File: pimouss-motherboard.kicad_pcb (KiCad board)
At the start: 4 copper layers, 281 parts, among them J1 Conn_02x10_Odd_Even, J10 Barrel_Jack_Switch, J2 TMS-105-57-GD, J3 Conn_02x10_Odd_Even, J4 Conn_01x03_Male, J5 Micro_SD_Card_Det, J9 RJSAE-5x8, P1 QSH-060-01-L-D-A, P2 PCIE-064-02, P3 MPCIE-Socket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

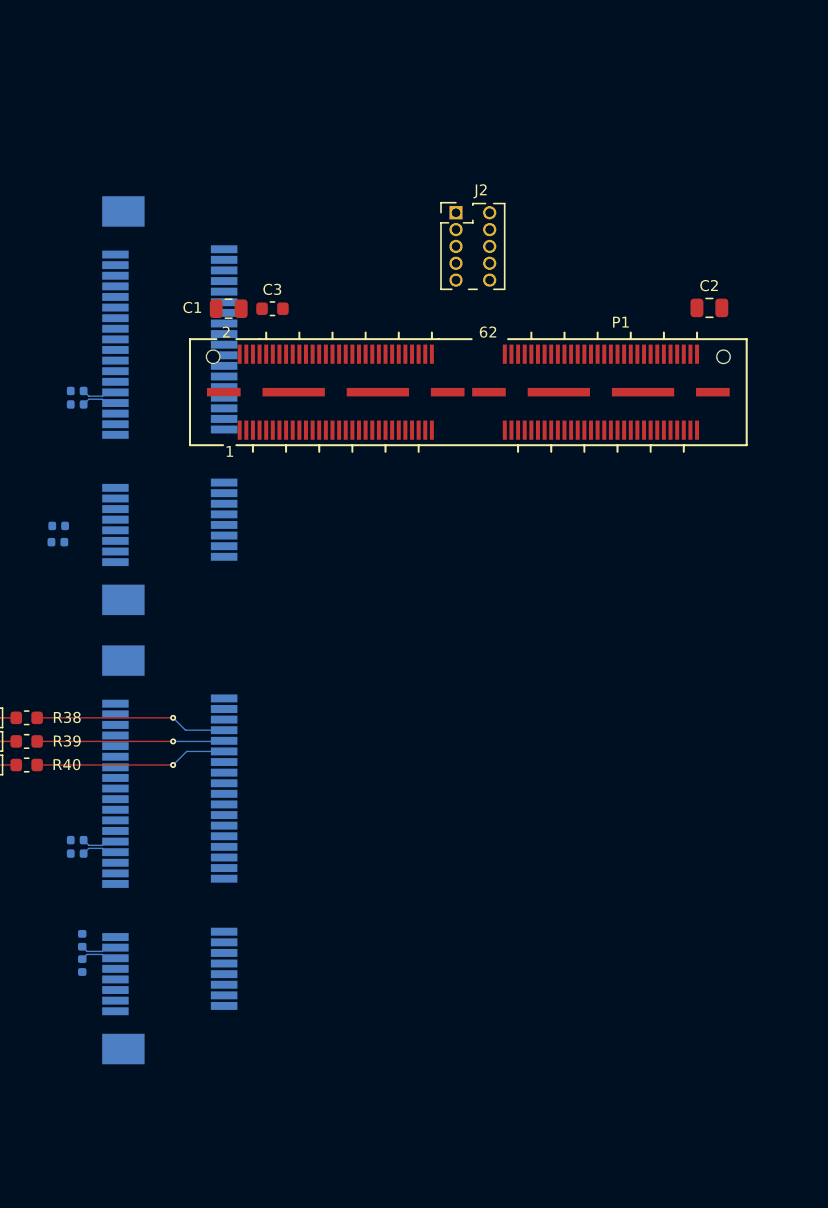
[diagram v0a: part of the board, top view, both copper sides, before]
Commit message: sch, master: Add pimouss SoM component
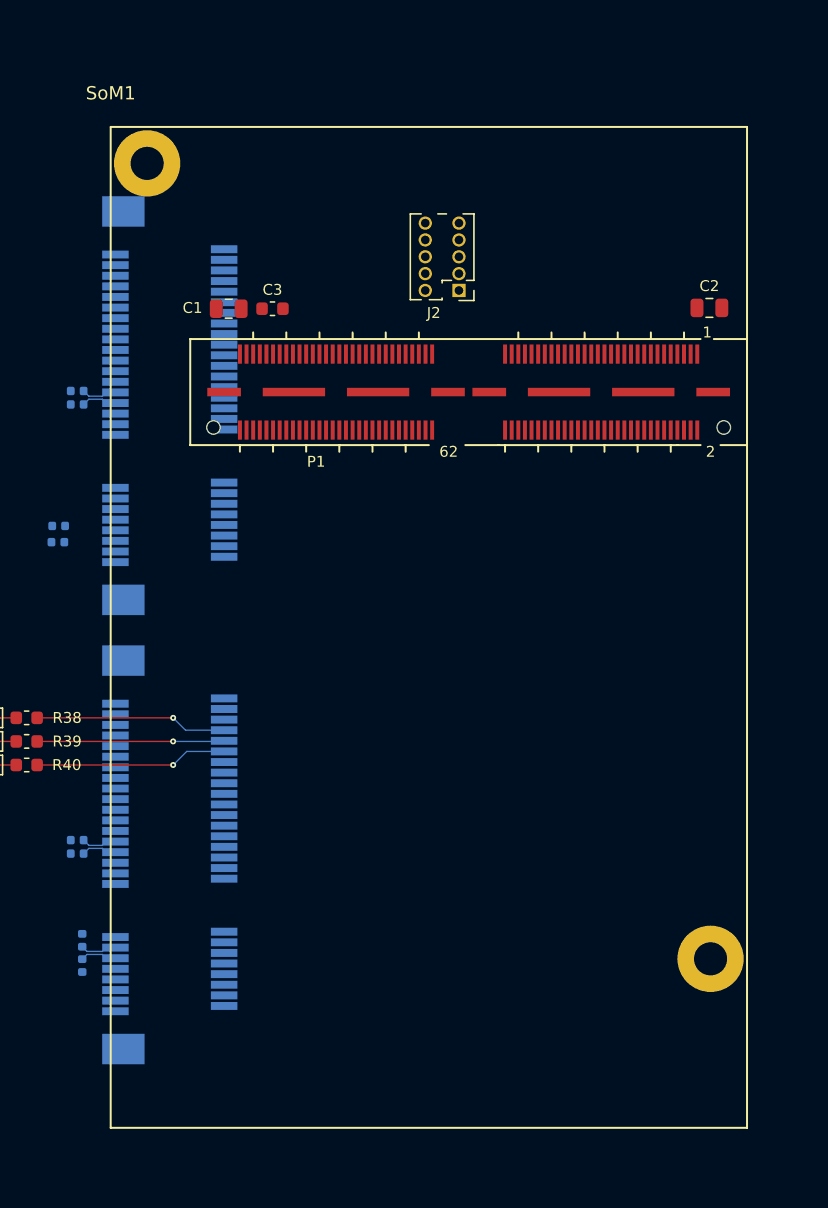
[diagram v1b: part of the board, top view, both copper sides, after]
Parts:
- added SoM1: Pimouss, pimouss-motherboard:Pimouss, F.Cu at (131.9, 58.7)
- moved J2 2.45 mm to (129.9, 48.5), turned to 180 degrees
- turned P1 to 180 degrees

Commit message: pcb: Place all components on the board
only routing left...
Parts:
- removed C14, C17, C21, C22, C24, C25: 1u, Capacitor_SMD:C_0603_1608Metric
- removed L3, L5, L6: 600@100M, Inductor_SMD:L_0603_1608Metric
- removed Q1: DMP2040USS, Package_SO:SOIC-8_3.9x4.9mm_P1.27mm
- added REF**: mpcie_card_left, pimouss-motherboard:mpcie_card_left, B.Cu at (103.9, 73.4)
- added REF**: mpcie_card_left, pimouss-motherboard:mpcie_card_left, B.Cu at (103.9, 107.3)
- added REF**: pcie_x4_card, pimouss-motherboard:pcie_x4_card, F.Cu at (162.6, 80.8)
- added REF**: PTH_3.3_6, pimouss-motherboard:PTH_3.3_6, F.Cu at (163.9, 26.3)
- added REF**: PTH_3.3_6, pimouss-motherboard:PTH_3.3_6, F.Cu at (163.9, 138.3)
- added REF**: PTH_3.3_6, pimouss-motherboard:PTH_3.3_6, F.Cu at (101.9, 138.3)
- added REF**: PTH_3.3_6, pimouss-motherboard:PTH_3.3_6, F.Cu at (101.9, 26.3)
- C20, C23, C40, C49, C50, C51, C52, C53, C54, C55, C56, L10, L11, L12, L4, L9: moved to B.Cu
- moved R4 164.8 mm to (114.5, 69.5), turned to 180 degrees
- moved R3 161.0 mm to (111.2, 67.9)
- moved R5 160.4 mm to (114.5, 71.4), turned to 180 degrees
- moved C108 157.1 mm to (120.3, 49.6), turned to 270 degrees
- moved R74 155.9 mm to (122.6, 50.3), turned to 180 degrees
- moved C112 155.6 mm to (122.6, 48.8), turned to 180 degrees
- moved R7 154.7 mm to (114.5, 66.6)
- moved C106 146.8 mm to (127.8, 43.3), turned to 270 degrees
- moved R9 145.3 mm to (121.0, 66.2)
- moved P5 144.1 mm to (112.6, 22.0), turned to 180 degrees
- moved R8 143.4 mm to (121.0, 64.7)
- moved R75 143.3 mm to (122.6, 51.8)
- moved U1 143.1 mm to (111.1, 70.5)
- moved C36 142.1 mm to (111.6, 32.4), turned to 180 degrees
- moved R10 141.6 mm to (128.1, 53.1)
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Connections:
- C120 pad 1: /pcie/switch/VDDR -> /pcie/switch/AVDDH
- C122 pad 1: /pcie/switch/VDDR -> /pcie/switch/AVDDH
- C124 pad 1: /pcie/switch/VDDR -> /pcie/switch/AVDDH
- C126 pad 1: /pcie/switch/VDDR -> /pcie/switch/AVDDH
- C128 pad 1: /pcie/switch/VDDR -> /pcie/switch/AVDDH
- C130 pad 1: /pcie/switch/VDDR -> /pcie/switch/AVDDH
- C139 pad 1: /pcie/switch/VDDCAUX -> /pcie/switch/AVDD
- C141 pad 1: /pcie/switch/VDDCAUX -> /pcie/switch/AVDD
- C143 pad 1: /pcie/switch/VDDCAUX -> /pcie/switch/AVDD
- C145 pad 1: /pcie/switch/CVDDR -> /pcie/switch/AVDDH
- C147 pad 1: /pcie/switch/CVDDR -> /pcie/switch/AVDDH
- C149 pad 1: /pcie/switch/CVDDR -> /pcie/switch/AVDDH
- C150 pad 1: /pcie/switch/CVDDR -> /pcie/switch/AVDDH
- C16 pad 1: /pcie/switch/VDDCAUX -> /pcie/switch/AVDD
- C23 pad 1: /pcie/switch/VDDR -> /pcie/switch/AVDDH
- J10 pad 1: Net-(J10-Pad1) -> +12V
- L2 pad 2: /pcie/switch/VDDCAUX -> /pcie/switch/AVDD
- L4 pad 2: /pcie/switch/VDDR -> /pcie/switch/AVDDH
- U2 pad 1: /pcie/switch/VDDR -> /pcie/switch/AVDDH
- U2 pad 13: /pcie/switch/VDDCAUX -> /pcie/switch/AVDD
- U2 pad 14: /pcie/switch/VDDCAUX -> /pcie/switch/AVDD
- U2 pad 49: /pcie/switch/VDDR -> /pcie/switch/AVDDH
- U2 pad 64: /pcie/switch/VDDR -> /pcie/switch/AVDDH
- U2 pad 79: /pcie/switch/CVDDR -> /pcie/switch/AVDDH
- U2 pad 8: /pcie/switch/VDDR -> /pcie/switch/AVDDH
- U2 pad 82: /pcie/switch/CVDDR -> /pcie/switch/AVDDH
- U2 pad 84: /pcie/switch/CVDDR -> /pcie/switch/AVDDH
- U2 pad 96: /pcie/switch/VDDR -> /pcie/switch/AVDDH
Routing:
- net /pcie/TX_O2_N: track 0.00 -> 60.4 mm
- net /pcie/TX_O2_P: track 0.00 -> 60.3 mm
- net /pcie/switch/AVDDH: track 23.1 -> 82.9 mm, vias 2 -> 11
- net /pcie/CLK_O2_N: track 0.00 -> 58.8 mm, vias 0 -> 2
- net /pcie/CLK_O2_P: track 0.00 -> 58.0 mm, vias 0 -> 2
- net /pcie/switch/VDDR: track 55.4 -> 0.00 mm, vias 5 -> 0
- net /pcie/CLK_O1_N: track 2.77 -> 39.0 mm
- net /pcie/CLK_O1_P: track 2.77 -> 38.6 mm
- net /phy_adm/REF_CLK_P: track 0.00 -> 32.9 mm
- net /phy_adm/REF_CLK_N: track 0.00 -> 32.8 mm
- net /pcie/TX_O1_N: track 0.00 -> 31.8 mm
- net /pcie/TX_O1_P: track 0.00 -> 31.1 mm
- net /pcie/switch/REFCLK_N: track 6.79 -> 33.5 mm, vias 0 -> 2
- net /pcie/switch/REFCLK_P: track 6.79 -> 32.3 mm, vias 0 -> 2
- net /pcie/RX_O2_P: track 6.75 -> 31.7 mm
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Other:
- board outline added: 70 x 120 mm

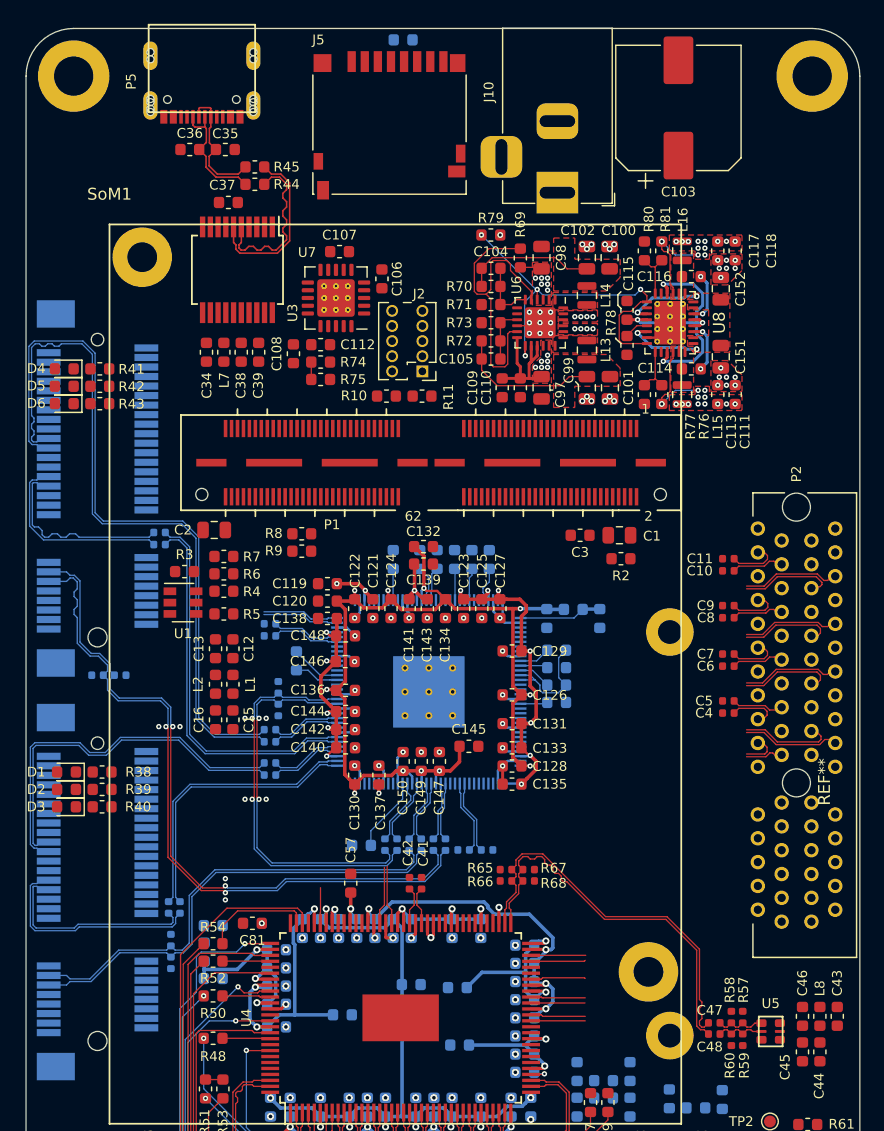
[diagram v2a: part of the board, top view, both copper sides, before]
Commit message: pcb: Routed PCIe differential tracks
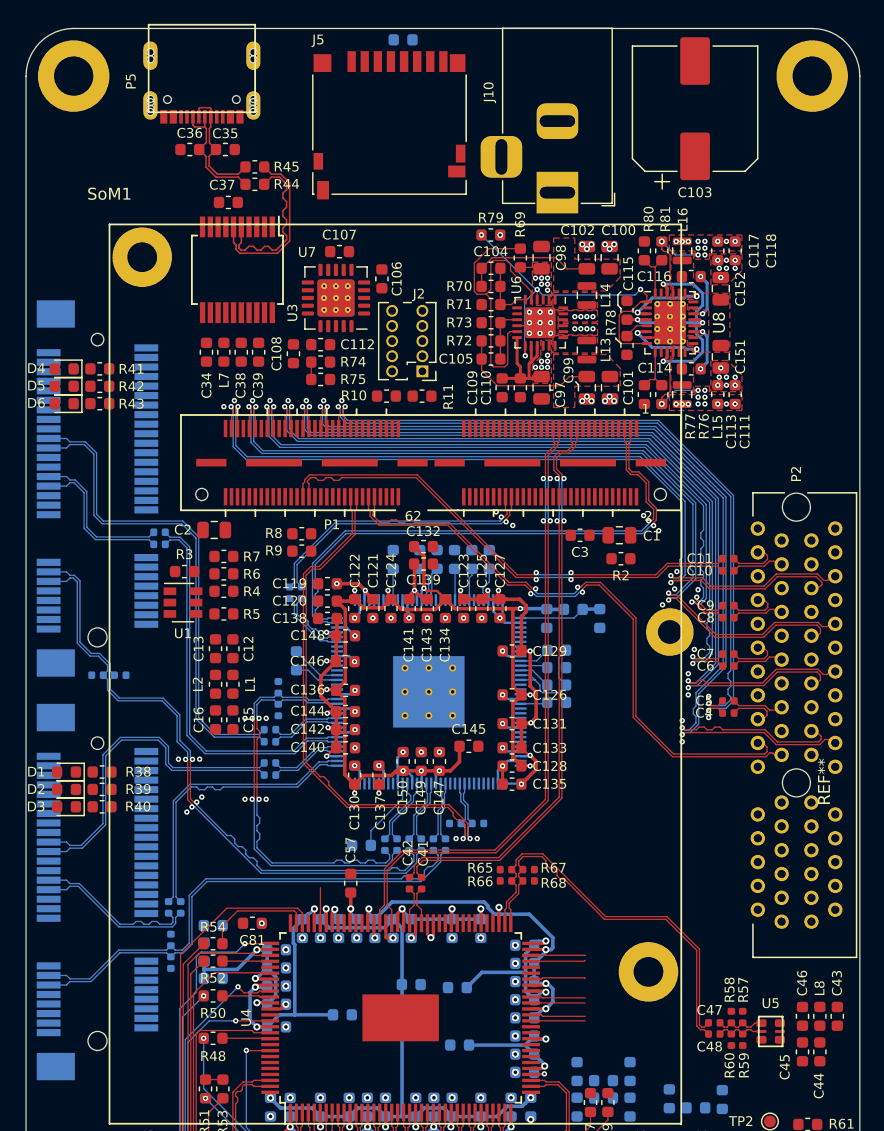
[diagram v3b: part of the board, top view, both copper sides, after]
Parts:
- removed the REF** at (103.9, 107.3)
- moved R24 24.9 mm to (103.9, 76.6), turned to 180 degrees
- moved R22 24.9 mm to (110.0, 100.7), turned to 270 degrees
- moved R25 22.6 mm to (105.8, 76.6), turned to 0 degrees
- moved R23 22.6 mm to (110.0, 98.8), turned to 90 degrees
- moved C19 3.98 mm to (120.0, 69.7), turned to 90 degrees
- moved C18 3.73 mm to (121.0, 69.7), turned to 90 degrees
- moved R14 2.35 mm to (135.8, 89.0)
- moved R16 2.33 mm to (133.9, 89.0)
- moved C103 1.40 mm to (154.1, 29.0)
- moved C32 1.04 mm to (109.1, 64.6)
- moved C31 1.02 mm to (110.9, 96.1)
- moved C33 1.00 mm to (109.1, 65.6)
- moved C30 0.95 mm to (109.9, 96.1)
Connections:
- C30 pad 1: /pcie/RX_O1_P -> /pcie/RX_O1_N
- C31 pad 1: /pcie/RX_O1_N -> /pcie/RX_O1_P
- C32 pad 1: /pcie/RX_O2_P -> /pcie/RX_O2_N
- C33 pad 1: /pcie/RX_O2_N -> /pcie/RX_O2_P
- P3 pad 31: /pcie/TX_O1_N -> /pcie/TX_O1_P
- P3 pad 33: /pcie/TX_O1_P -> /pcie/TX_O1_N
- P4 pad 31: /pcie/TX_O2_N -> /pcie/TX_O2_P
- P4 pad 33: /pcie/TX_O2_P -> /pcie/TX_O2_N
- R18 pad 2: /pcie/CLK_O1_P -> /pcie/CLK_O2_P
- R19 pad 2: /pcie/CLK_O1_N -> /pcie/CLK_O2_N
- R20 pad 2: /pcie/CLK_O2_P -> /pcie/CLK_O1_P
- R21 pad 2: /pcie/CLK_O2_N -> /pcie/CLK_O1_N
- R22 pad 1: /pcie/CLK_O2_N -> /pcie/CLK_O1_N
- R23 pad 1: /pcie/CLK_O2_P -> /pcie/CLK_O1_P
- R24 pad 1: /pcie/CLK_O1_N -> /pcie/CLK_O2_N
- R25 pad 1: /pcie/CLK_O1_P -> /pcie/CLK_O2_P
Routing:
- net /PCIE_X4_TX0_N: track 8.02 -> 75.1 mm, vias 0 -> 2
- net /PCIE_X4_TX0_P: track 8.17 -> 75.0 mm, vias 0 -> 2
- net /PCIE_X4_TX1_P: track 8.05 -> 71.1 mm, vias 0 -> 2
- net /PCIE_X4_TX1_N: track 8.20 -> 71.1 mm, vias 0 -> 2
- net /PCIE_X4_TX2_P: track 7.97 -> 69.5 mm, vias 0 -> 2
- net /PCIE_X4_TX2_N: track 8.11 -> 69.5 mm, vias 0 -> 2
- net /PCIE_X4_RX1_P: track 0.00 -> 59.5 mm, vias 0 -> 2
- net /PCIE_X4_RX1_N: track 0.00 -> 59.5 mm, vias 0 -> 2
- net /PCIE_X4_RX0_P: track 0.00 -> 59.4 mm, vias 0 -> 2
- net /PCIE_X4_RX0_N: track 0.00 -> 59.4 mm, vias 0 -> 2
- net /PCIE_X4_TX3_P: track 8.14 -> 67.4 mm, vias 0 -> 2
- net /PCIE_X4_TX3_N: track 8.24 -> 67.4 mm, vias 0 -> 2
- net /PCIE_X4_RX2_P: track 0.00 -> 55.8 mm, vias 0 -> 2
- net /PCIE_X4_RX2_N: track 0.00 -> 55.8 mm, vias 0 -> 2
- net /QSGMII_TX_P: track 0.00 -> 48.2 mm, vias 0 -> 2
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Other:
- net class Default: clearance 0.127 -> 0.1; trace_width 0.1016 -> 0.1
- rule trace_clearance: 0.127 -> 0.1

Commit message: pcb: ROUTE ALL THE THINGS
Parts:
- removed SoM1: Pimouss, pimouss-motherboard:Pimouss
- added REF**: mpcie_card_left, pimouss-motherboard:mpcie_card_left, B.Cu at (103.9, 107.3)
- moved R11 28.4 mm to (102.9, 55.8)
- moved R10 25.6 mm to (102.9, 57.2), turned to 180 degrees
- moved R8 19.1 mm to (102.9, 58.7), turned to 180 degrees
- moved R9 19.1 mm to (102.9, 60.1), turned to 180 degrees
- moved R2 11.2 mm to (154.7, 57.9)
- moved R61 2.86 mm to (163.5, 117.2)
- moved C3 2.85 mm to (147.0, 63.7)
- moved R55 2.79 mm to (163.5, 123.2)
- moved R56 2.79 mm to (163.5, 124.7)
- moved R62 2.79 mm to (163.5, 121.7)
- moved R63 2.79 mm to (163.5, 120.1)
- moved R64 2.79 mm to (163.5, 118.6)
- moved C48 1.81 mm to (154.7, 105.2), turned to 315 degrees
- moved C47 1.29 mm to (155.4, 104.5), turned to 315 degrees
- moved C40 0.95 mm to (129.5, 24.2)
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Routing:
- net +3V3: track 58.7 -> 464.4 mm, vias 5 -> 29
- net +3V3_PCI: track 11.1 -> 271.1 mm, vias 0 -> 27
- net /SMB_DATA: track 0.00 -> 181.9 mm, vias 0 -> 7
- net /SMB_CLK: track 0.00 -> 177.3 mm, vias 0 -> 8
- net /nRST: track 2.98 -> 174.2 mm, vias 0 -> 3
- net +1V5_PCI: track 12.2 -> 132.2 mm, vias 0 -> 26
- net /pimouss/BSTRAP: track 0.00 -> 111.1 mm
- net /pimouss/MPP22: track 0.00 -> 98.9 mm, vias 0 -> 1
- net +1V8: track 3.66 -> 98.7 mm, vias 1 -> 30
- net /pimouss/MPP47: track 0.00 -> 93.4 mm, vias 0 -> 1
- net /pimouss/MPP49: track 0.00 -> 90.9 mm, vias 0 -> 1
- net /pimouss/JTDO: track 0.00 -> 86.7 mm
- net Net-(J3-Pad15): track 0.00 -> 84.1 mm
- net /pimouss/JTCK: track 0.00 -> 79.4 mm
- net /pimouss/MPP23: track 0.00 -> 77.9 mm, vias 0 -> 1
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- added copper zone on In2.Cu, net +12V
- added copper zone on F.Cu, net +1V0
- added copper zone on B.Cu, net +1V8
- added copper zone on F.Cu, net +1V8
- added copper zone on In1.Cu, net +1V8
- added copper zone on B.Cu, net +3V3
- added copper zone on F.Cu, net +3V3
- added copper zone on B.Cu, net +3V3_PCI
- added copper zone on B.Cu, net GND
- added copper zone on In1.Cu, net GND
- added copper zone on In2.Cu, net GND
- added copper zone on F.Cu, net Net-(C44-Pad2)
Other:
- net class Power: clearance 0.127 -> 0.1
- net class Power PCIe sw: clearance 0.127 -> 0.1
